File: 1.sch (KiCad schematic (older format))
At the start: 46 parts, among them J1 Micro_SD_Card, J10 BxI2C1, J11 I2C2, J2 USB_B_Micro, J3 Power, J4 SWD, J5 Protected, J6 SPI1, J7 ADC, J8 UART1, J9 SPI2, K1 NRST, K2 WKUP, K3 KPA0, U1 STM32F103C8Tx, U2 AMS1117-3.3, Y1 8MHz, Y2 32.768k

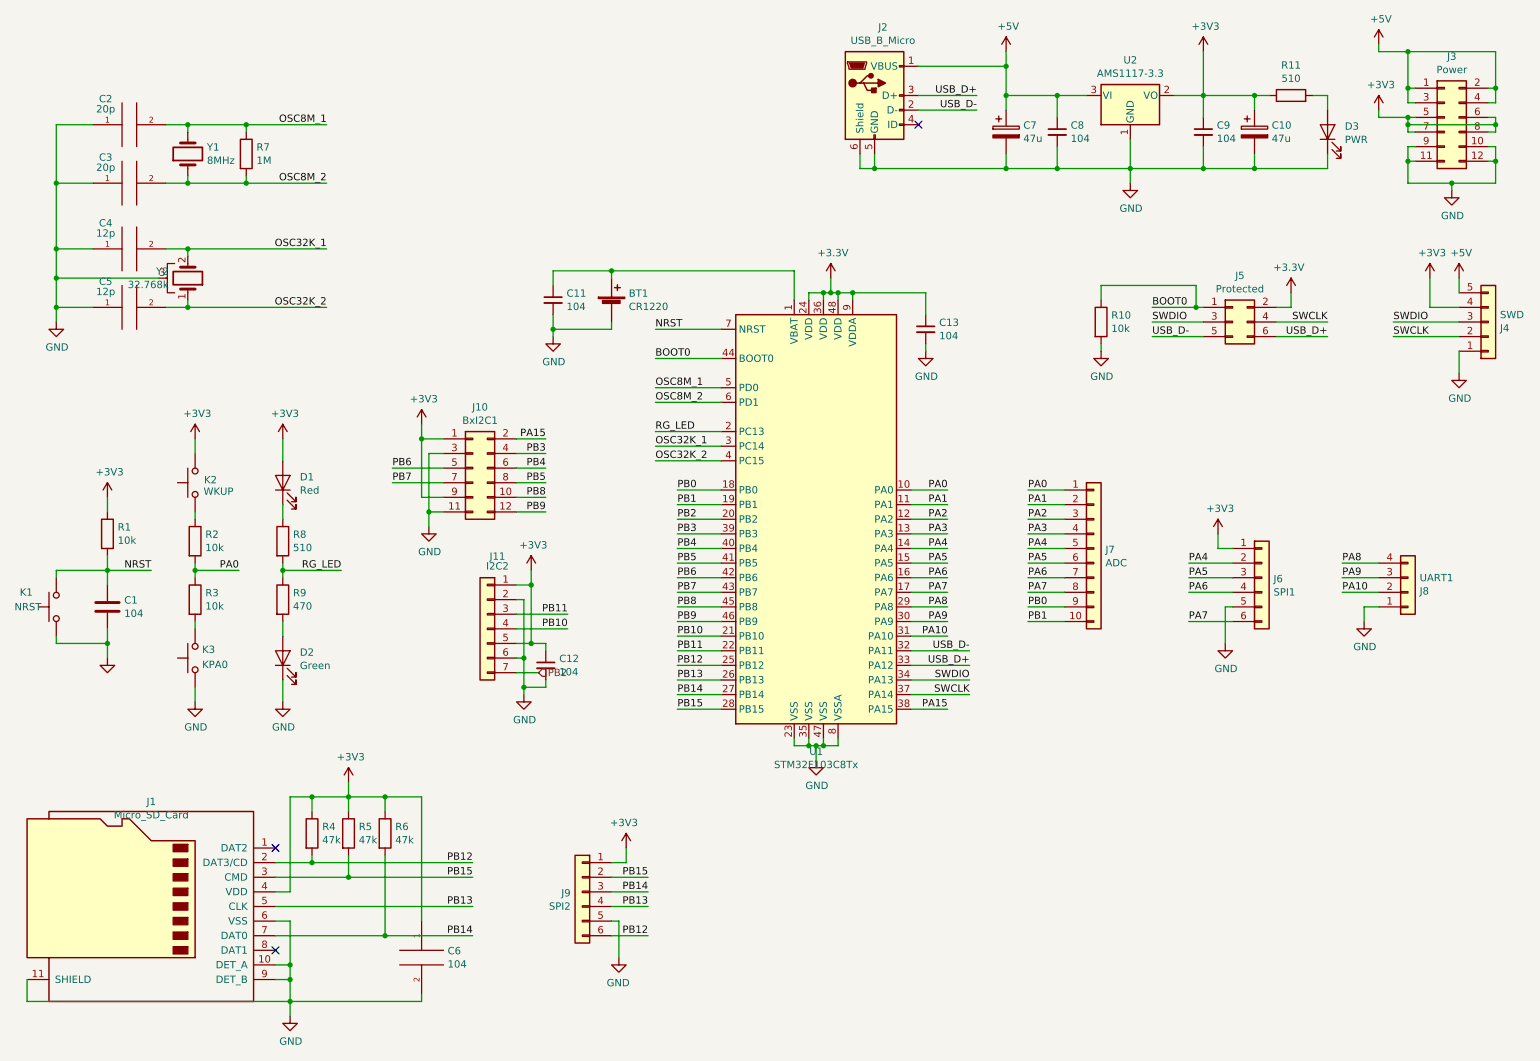
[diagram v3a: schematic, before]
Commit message: 修改原理图字段，并修改PCB
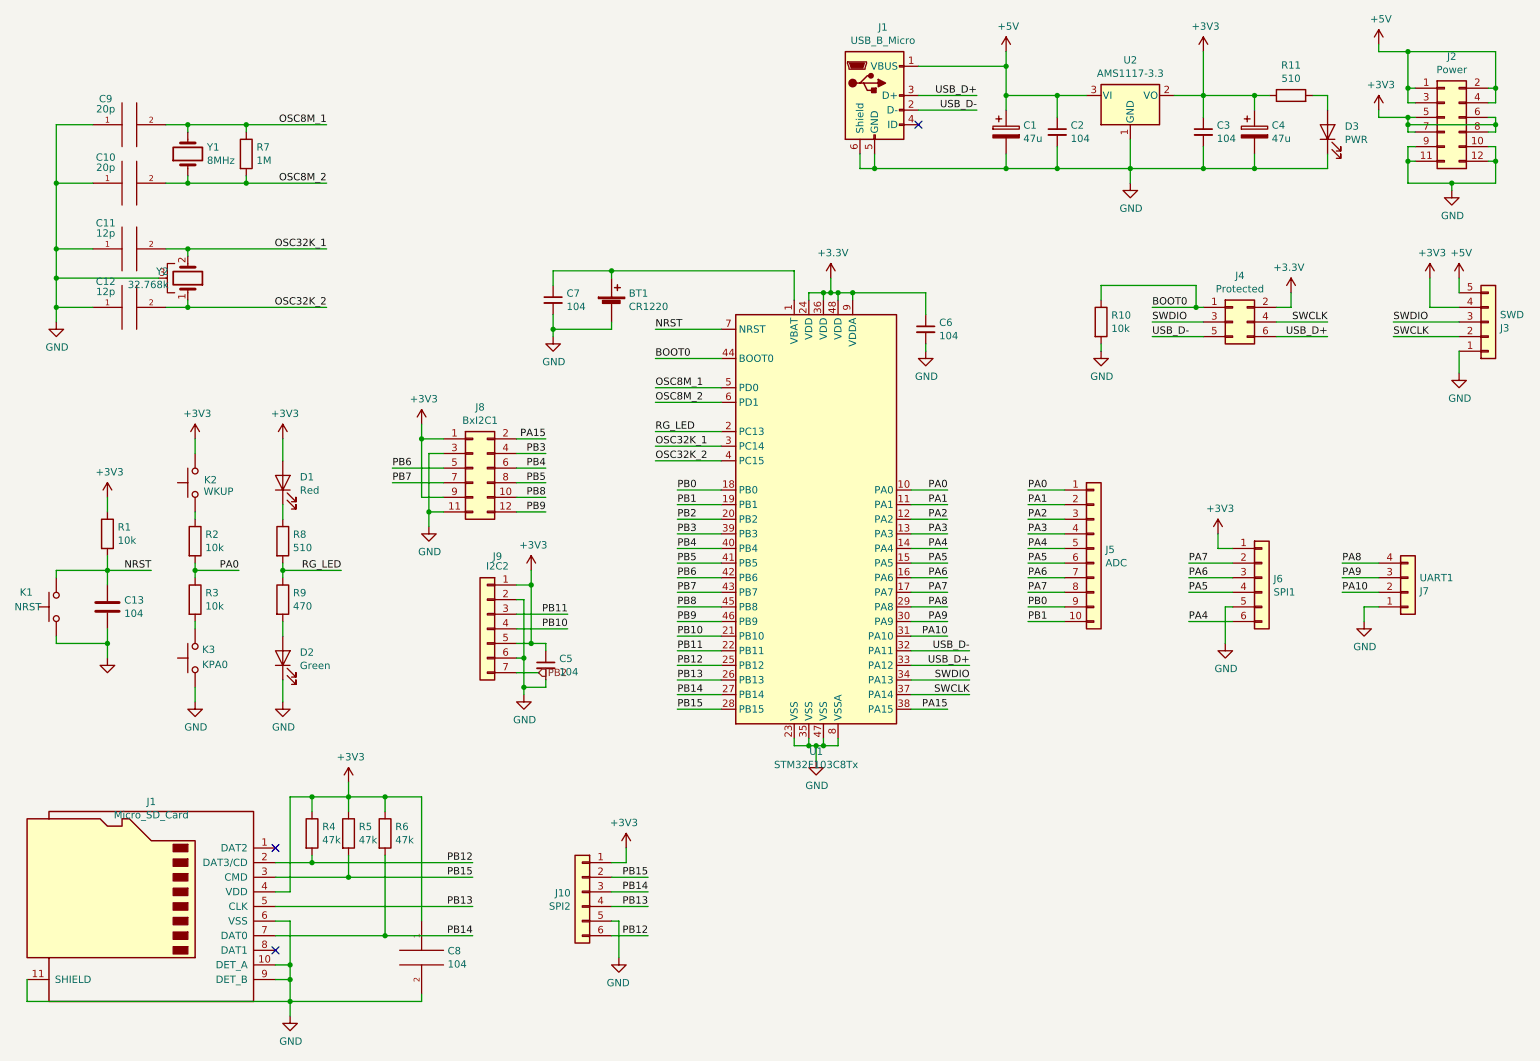
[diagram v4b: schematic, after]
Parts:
- C5: renamed from C12; footprint Capacitor_SMD:C_0201_0603Metric -> Capacitor_SMD:C_0603_1608Metric
- renumbered C7 to C1, C3 to C10, C4 to C11, C5 to C12, C1 to C13, C8 to C2, C9 to C3, C10 to C4, C13 to C6, C11 to C7, C6 to C8, C2 to C9, J2 to J1, J9 to J10, J3 to J2, J4 to J3, J5 to J4, J7 to J5, J8 to J7, J10 to J8, J11 to J9
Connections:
- net PA4: now also J6.6 (Pin_6); no longer J6.2 (Pin_2)
- net PA5: now also J6.4 (Pin_4); no longer J6.3 (Pin_3)
- net PA6: now also J6.3 (Pin_3); no longer J6.4 (Pin_4)
- net PA7: now also J6.2 (Pin_2); no longer J6.6 (Pin_6)
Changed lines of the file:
@@
 $EndComp
 $Comp
-L Device:C C1
+L Device:C C13
 U 1 1 60803DC4
 P 1350 4750
-F 0 "C1" H 1465 4796 50  0000 L CNN
+F 0 "C13" H 1465 4796 50  0000 L CNN
 F 1 "104" H 1465 4705 50  0000 L CNN
 F 2 "Capacitor_SMD:C_0603_1608Metric" H 1388 4600 50  0001 C CNN
@@
 	1250 1450 1000 1450
 $Comp
-L pspice:CAP C2
+L pspice:CAP C9
 U 1 1 60899DE9
 P 1500 1450
-F 0 "C2" V 1706 1612 50  0000 C BNN
+F 0 "C9" V 1706 1612 50  0000 C BNN
 F 1 "20p" V 1607 1612 50  0000 C CNN
 F 2 "Capacitor_SMD:C_0603_1608Metric" H 1500 1450 50  0001 C CNN
@@
 	1000 1450 1000 1850
 $Comp
-L pspice:CAP C3
+L pspice:CAP C10
 U 1 1 6092BDFE
 P 1500 1850
-F 0 "C3" V 1706 2012 50  0000 C BNN
+F 0 "C10" V 1706 2012 50  0000 C BNN
 F 1 "20p" V 1607 2012 50  0000 C CNN
 F 2 "Capacitor_SMD:C_0603_1608Metric" H 1500 1850 50  0001 C CNN
@@
 $EndComp
 $Comp
-L pspice:CAP C4
+L pspice:CAP C11
 U 1 1 6092C5E0
 P 1500 2300
-F 0 "C4" V 1706 2462 50  0000 C BNN
+F 0 "C11" V 1706 2462 50  0000 C BNN
 F 1 "12p" V 1607 2462 50  0000 C CNN
 F 2 "Capacitor_SMD:C_0603_1608Metric" H 1500 2300 50  0001 C CNN
@@
 $EndComp
 $Comp
-L pspice:CAP C5
+L pspice:CAP C12
 U 1 1 6092D115
 P 1500 2700
-F 0 "C5" V 1706 2862 50  0000 C BNN
+F 0 "C12" V 1706 2862 50  0000 C BNN
 F 1 "12p" V 1607 2862 50  0000 C CNN
 F 2 "Capacitor_SMD:C_0603_1608Metric" H 1500 2700 50  0001 C CNN
@@
 Connection ~ 3250 6050
 $Comp
-L pspice:C C6
+L pspice:C C8
 U 1 1 60A0DA04
 P 3500 7150
-F 0 "C6" H 3678 7196 50  0000 L CNN
+F 0 "C8" H 3678 7196 50  0000 L CNN
 F 1 "104" H 3678 7105 50  0000 L CNN
 F 2 "Capacitor_SMD:C_0603_1608Metric" H 3500 7150 50  0001 C CNN
@@
 $EndComp
 $Comp
-L Connector_Generic:Conn_02x03_Odd_Even J5
+L Connector_Generic:Conn_02x03_Odd_Even J4
 U 1 1 608D3B31
 P 9050 2800
-F 0 "J5" H 9100 3117 50  0000 C CNN
+F 0 "J4" H 9100 3117 50  0000 C CNN
 F 1 "Protected" H 9100 3026 50  0000 C CNN
 F 2 "Connector_PinHeader_2.54mm:PinHeader_2x03_P2.54mm_Vertical" H 9050 2800 50  0001 C CNN
@@
 	9000 4750 9000 5000
 $Comp
-L Connector_Generic:Conn_01x10 J7
+L Connector_Generic:Conn_01x10 J5
 U 1 1 60BF7B89
 P 8100 4350
-F 0 "J7" H 8180 4342 50  0000 L CNN
+F 0 "J5" H 8180 4342 50  0000 L CNN
 F 1 "ADC" H 8180 4251 50  0000 L CNN
 F 2 "Connector_PinHeader_2.54mm:PinHeader_1x10_P2.54mm_Vertical" H 8100 4350 50  0001 C CNN
@@
 $EndComp
 $Comp
-L Connector_Generic:Conn_01x04 J8
+L Connector_Generic:Conn_01x04 J7
 U 1 1 60F3F899
 P 10250 4650
-F 0 "J8" H 10330 4642 50  0000 L CNN
+F 0 "J7" H 10330 4642 50  0000 L CNN
 F 1 "UART1" H 10330 4551 50  0000 L CNN
 F 2 "Connector_PinHeader_2.54mm:PinHeader_1x04_P2.54mm_Vertical" H 10250 4650 50  0001 C CNN
@@
 $EndComp
 $Comp
-L Device:C_Small C11
+L Device:C_Small C7
 U 1 1 6096DC0F
 P 4400 2650
-F 0 "C11" H 4492 2696 50  0000 L CNN
+F 0 "C7" H 4492 2696 50  0000 L CNN
 F 1 "104" H 4492 2605 50  0000 L CNN
 F 2 "Capacitor_SMD:C_0603_1608Metric" H 4400 2650 50  0001 C CNN
@@
 	4400 2850 4400 2900
 $Comp
-L Device:C_Small C13
+L Device:C_Small C6
 U 1 1 60A78AA2
 P 6950 2850
-F 0 "C13" H 7042 2896 50  0000 L CNN
+F 0 "C6" H 7042 2896 50  0000 L CNN
 F 1 "104" H 7042 2805 50  0000 L CNN
 F 2 "Capacitor_SMD:C_0603_1608Metric" H 6950 2850 50  0001 C CNN
@@
 	10600 2500 10600 2600
 $Comp
-L Connector_Generic:Conn_01x05 J4
+L Connector_Generic:Conn_01x05 J3
 U 1 1 60DF5E87
 P 10800 2800
-F 0 "J4" H 10880 2842 50  0000 L CNN
+F 0 "J3" H 10880 2842 50  0000 L CNN
 F 1 "SWD" H 10880 2751 50  0000 L CNN
 F 2 "Connector_PinHeader_2.54mm:PinHeader_1x05_P2.54mm_Horizontal" H 10800 2800 50  0001 C CNN
@@
 $EndComp
 $Comp
-L Connector_Generic:Conn_02x06_Odd_Even J3
+L Connector_Generic:Conn_02x06_Odd_Even J2
 U 1 1 60CA00CD
 P 10500 1400
-F 0 "J3" H 10550 1817 50  0000 C CNN
+F 0 "J2" H 10550 1817 50  0000 C CNN
 F 1 "Power" H 10550 1726 50  0000 C CNN
 F 2 "Connector_PinHeader_2.54mm:PinHeader_2x06_P2.54mm_Vertical" H 10500 1400 50  0001 C CNN
@@
 $EndComp
 $Comp
-L Connector:USB_B_Micro J2
+L Connector:USB_B_Micro J1
 U 1 1 60B0F0BF
 P 6600 1250
-F 0 "J2" H 6657 1717 50  0000 C CNN
+F 0 "J1" H 6657 1717 50  0000 C CNN
 F 1 "USB_B_Micro" H 6657 1626 50  0000 C CNN
 F 2 "Connector_USB:USB_Micro-B_GCT_USB3076-30-A" H 6750 1200 50  0001 C CNN
@@
 	8650 1250 8850 1250
 $Comp
-L Device:CP C10
+L Device:CP C4
 U 1 1 60B9D540
 P 9200 1500
-F 0 "C10" H 9318 1546 50  0000 L CNN
+F 0 "C4" H 9318 1546 50  0000 L CNN
 F 1 "47u" H 9318 1455 50  0000 L CNN
 F 2 "Capacitor_SMD:C_1206_3216Metric" H 9238 1350 50  0001 C CNN
@@
 	7850 1250 7850 1400
 $Comp
-L Device:C_Small C9
+L Device:C_Small C3
 U 1 1 60B7BA0C
 P 8850 1500
-F 0 "C9" H 8942 1546 50  0000 L CNN
+F 0 "C3" H 8942 1546 50  0000 L CNN
 F 1 "104" H 8942 1455 50  0000 L CNN
 F 2 "Capacitor_SMD:C_0603_1608Metric" H 8850 1500 50  0001 C CNN
@@
 $EndComp
 $Comp
-L Device:C_Small C8
+L Device:C_Small C2
 U 1 1 60B7A582
 P 7850 1500
-F 0 "C8" H 7942 1546 50  0000 L CNN
+F 0 "C2" H 7942 1546 50  0000 L CNN
 F 1 "104" H 7942 1455 50  0000 L CNN
 F 2 "Capacitor_SMD:C_0603_1608Metric" H 7850 1500 50  0001 C CNN
@@
 $EndComp
 $Comp
-L Device:CP C7
+L Device:CP C1
 U 1 1 60B79A0D
 P 7500 1500
-F 0 "C7" H 7618 1546 50  0000 L CNN
+F 0 "C1" H 7618 1546 50  0000 L CNN
 F 1 "47u" H 7618 1455 50  0000 L CNN
 F 2 "Capacitor_SMD:C_1206_3216Metric" H 7538 1350 50  0001 C CNN
@@
 	3500 3600 3650 3600
 $Comp
-L Connector_Generic:Conn_02x06_Odd_Even J10
+L Connector_Generic:Conn_02x06_Odd_Even J8
 U 1 1 60B34FEB
 P 3850 3800
-F 0 "J10" H 3900 4217 50  0000 C CNN
+F 0 "J8" H 3900 4217 50  0000 C CNN
 F 1 "BxI2C1" H 3900 4126 50  0000 C CNN
 F 2 "Connector_PinHeader_2.54mm:PinHeader_2x06_P2.54mm_Vertical" H 3850 3800 50  0001 C CNN
@@
 	4800 6900 4850 6900
 $Comp
-L Connector_Generic:Conn_01x06 J9
+L Connector_Generic:Conn_01x06 J10
 U 1 1 61009C91
 P 4600 6700
-F 0 "J9" H 4680 6692 50  0000 L CNN
+F 0 "J10" H 4680 6692 50  0000 L CNN
 F 1 "SPI2" H 4680 6601 50  0000 L CNN
 F 2 "Connector_PinHeader_2.54mm:PinHeader_1x06_P2.54mm_Vertical" H 4680 6555 50  0001 L CNN
@@
 	4350 5050 4350 5000
 $Comp
-L Device:C_Small C12
+L Device:C_Small C5
 U 1 1 609EBE25
 P 4350 5150
-F 0 "C12" H 4442 5196 50  0000 L CNN
+F 0 "C5" H 4442 5196 50  0000 L CNN
 F 1 "104" H 4442 5105 50  0000 L CNN
-F 2 "Capacitor_SMD:C_0201_0603Metric" H 4350 5150 50  0001 C CNN
+F 2 "Capacitor_SMD:C_0603_1608Metric" H 4350 5150 50  0001 C CNN
 F 3 "~" H 4350 5150 50  0001 C CNN
 	1    4350 5150
@@
 	4150 5100 4200 5100
 $Comp
-L Connector_Generic:Conn_01x07 J11
+L Connector_Generic:Conn_01x07 J9
 U 1 1 6153FBE5
 P 3950 4900
-F 0 "J11" H 3881 5396 50  0000 C CNN
+F 0 "J9" H 3881 5396 50  0000 C CNN
 F 1 "I2C2" H 3881 5329 50  0000 C CNN
 F 2 "Connector_PinHeader_2.54mm:PinHeader_1x07_P2.54mm_Vertical" H 3950 4900 50  0001 C CNN
@@
 	7650 4850 7900 4850
 Text Label 8750 4450 0    50   ~ 0
+PA7
+Text Label 8750 4550 0    50   ~ 0
+PA6
+Text Label 8750 4650 0    50   ~ 0
+PA5
+Text Label 8750 4850 0    50   ~ 0
 PA4
-Text Label 8750 4550 0    50   ~ 0
-PA5
-Text Label 8750 4650 0    50   ~ 0
-PA6
-Text Label 8750 4850 0    50   ~ 0
-PA7
 Wire Wire Line
 	8750 4650 9050 4650

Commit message: 修改字段2
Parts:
- renumbered J1 to J11
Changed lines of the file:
@@
-$EndComp
-$Comp
-L power:GND #PWR0105
-U 1 1 608A3AFC
-P 1000 2800
-F 0 "#PWR0105" H 1000 2550 50  0001 C CNN
-F 1 "GND" H 1005 2627 50  0000 C CNN
-F 2 "" H 1000 2800 50  0001 C CNN
-F 3 "" H 1000 2800 50  0001 C CNN
-	1    1000 2800
-	1    0    0    -1
 $EndComp
 $Comp
@@
 	1750 1450 1900 1450
 Wire Wire Line
-	1250 1450 1000 1450
-$Comp
-L pspice:CAP C9
-U 1 1 60899DE9
-P 1500 1450
-F 0 "C9" V 1706 1612 50  0000 C BNN
-F 1 "20p" V 1607 1612 50  0000 C CNN
-F 2 "Capacitor_SMD:C_0603_1608Metric" H 1500 1450 50  0001 C CNN
-F 3 "~" H 1500 1450 50  0001 C CNN
-	1    1500 1450
-	0    -1   -1   0
-$EndComp
-Wire Wire Line
-	1000 1450 1000 1850
-$Comp
-L pspice:CAP C10
-U 1 1 6092BDFE
-P 1500 1850
-F 0 "C10" V 1706 2012 50  0000 C BNN
-F 1 "20p" V 1607 2012 50  0000 C CNN
-F 2 "Capacitor_SMD:C_0603_1608Metric" H 1500 1850 50  0001 C CNN
-F 3 "~" H 1500 1850 50  0001 C CNN
-	1    1500 1850
-	0    -1   -1   0
-$EndComp
-$Comp
-L pspice:CAP C11
-U 1 1 6092C5E0
-P 1500 2300
-F 0 "C11" V 1706 2462 50  0000 C BNN
-F 1 "12p" V 1607 2462 50  0000 C CNN
-F 2 "Capacitor_SMD:C_0603_1608Metric" H 1500 2300 50  0001 C CNN
-F 3 "~" H 1500 2300 50  0001 C CNN
-	1    1500 2300
-	0    -1   -1   0
-$EndComp
-$Comp
-L pspice:CAP C12
-U 1 1 6092D115
-P 1500 2700
-F 0 "C12" V 1706 2862 50  0000 C BNN
-F 1 "12p" V 1607 2862 50  0000 C CNN
-F 2 "Capacitor_SMD:C_0603_1608Metric" H 1500 2700 50  0001 C CNN
-F 3 "~" H 1500 2700 50  0001 C CNN
-	1    1500 2700
-	0    -1   -1   0
-$EndComp
-Wire Wire Line
-	1250 1850 1000 1850
-Connection ~ 1000 1850
-Wire Wire Line
-	1000 1850 1000 2300
-Wire Wire Line
-	1250 2300 1000 2300
-Connection ~ 1000 2300
-Wire Wire Line
-	1000 2300 1000 2500
-Wire Wire Line
-	1250 2700 1000 2700
-Connection ~ 1000 2700
-Wire Wire Line
-	1000 2700 1000 2800
-Wire Wire Line
 	2500 6600 3000 6600
 Wire Wire Line
@@
 	3500 6050 3500 6900
 Connection ~ 3250 6050
-$Comp
-L pspice:C C8
-U 1 1 60A0DA04
-P 3500 7150
-F 0 "C8" H 3678 7196 50  0000 L CNN
-F 1 "104" H 3678 7105 50  0000 L CNN
-F 2 "Capacitor_SMD:C_0603_1608Metric" H 3500 7150 50  0001 C CNN
-F 3 "~" H 3500 7150 50  0001 C CNN
-	1    3500 7150
-	1    0    0    -1
-$EndComp
 Wire Wire Line
 	2600 7450 3500 7450
@@
 	1750 2700 1900 2700
 $Comp
-L Connector:Micro_SD_Card_Det J1
+L Connector:Micro_SD_Card_Det J11
 U 1 1 60953440
 P 1600 6800
-F 0 "J1" H 1550 7517 50  0000 C CNN
+F 0 "J11" H 1550 7517 50  0000 C CNN
 F 1 "Micro_SD_Card" H 1550 7426 50  0000 C CNN
 F 2 "Connector_Card:microSD_HC_Hirose_DM3BT-DSF-PEJS" H 2750 7100 50  0001 C CNN
@@
 	-1   0    0    -1
 $EndComp
-Wire Wire Line
-	1700 2500 1000 2500
-Connection ~ 1000 2500
-Wire Wire Line
-	1000 2500 1000 2700
 Wire Wire Line
 	800  7300 800  7450
@@
 Wire Wire Line
 	9350 2900 9700 2900
+Wire Wire Line
+	1000 2500 1000 2700
+Connection ~ 1000 2500
+Wire Wire Line
+	1700 2500 1000 2500
+Wire Wire Line
+	1000 2700 1000 2800
+Connection ~ 1000 2700
+Wire Wire Line
+	1250 2700 1000 2700
+Wire Wire Line
+	1000 2300 1000 2500
+Connection ~ 1000 2300
+Wire Wire Line
+	1250 2300 1000 2300
+Wire Wire Line
+	1000 1850 1000 2300
+Connection ~ 1000 1850
+Wire Wire Line
+	1250 1850 1000 1850
+Wire Wire Line
+	1000 1450 1000 1850
+Wire Wire Line
+	1250 1450 1000 1450
+$Comp
+L power:GND #PWR0105
+U 1 1 608A3AFC
+P 1000 2800
+F 0 "#PWR0105" H 1000 2550 50  0001 C CNN
+F 1 "GND" H 1005 2627 50  0000 C CNN
+F 2 "" H 1000 2800 50  0001 C CNN
+F 3 "" H 1000 2800 50  0001 C CNN
+	1    1000 2800
+	1    0    0    -1
+$EndComp
+$Comp
+L pspice:CAP C12
+U 1 1 6092D115
+P 1500 2700
+F 0 "C12" V 1706 2862 50  0000 C BNN
+F 1 "12p" V 1607 2862 50  0000 C CNN
+F 2 "Capacitor_SMD:C_0603_1608Metric" H 1500 2700 50  0001 C CNN
+F 3 "~" H 1500 2700 50  0001 C CNN
+	1    1500 2700
+	0    -1   -1   0
+$EndComp
+$Comp
+L pspice:CAP C11
+U 1 1 6092C5E0
+P 1500 2300
+F 0 "C11" V 1706 2462 50  0000 C BNN
+F 1 "12p" V 1607 2462 50  0000 C CNN
+F 2 "Capacitor_SMD:C_0603_1608Metric" H 1500 2300 50  0001 C CNN
+F 3 "~" H 1500 2300 50  0001 C CNN
+	1    1500 2300
+	0    -1   -1   0
+$EndComp
+$Comp
+L pspice:CAP C10
+U 1 1 6092BDFE
+P 1500 1850
+F 0 "C10" V 1706 2012 50  0000 C BNN
+F 1 "20p" V 1607 2012 50  0000 C CNN
+F 2 "Capacitor_SMD:C_0603_1608Metric" H 1500 1850 50  0001 C CNN
+F 3 "~" H 1500 1850 50  0001 C CNN
+	1    1500 1850
+	0    -1   -1   0
+$EndComp
+$Comp
+L pspice:CAP C9
+U 1 1 60899DE9
+P 1500 1450
+F 0 "C9" V 1706 1612 50  0000 C BNN
+F 1 "20p" V 1607 1612 50  0000 C CNN
+F 2 "Capacitor_SMD:C_0603_1608Metric" H 1500 1450 50  0001 C CNN
+F 3 "~" H 1500 1450 50  0001 C CNN
+	1    1500 1450
+	0    -1   -1   0
+$EndComp
+$Comp
+L pspice:C C8
+U 1 1 60A0DA04
+P 3500 7150
+F 0 "C8" H 3678 7196 50  0000 L CNN
+F 1 "104" H 3678 7105 50  0000 L CNN
+F 2 "Capacitor_SMD:C_0603_1608Metric" H 3500 7150 50  0001 C CNN
+F 3 "~" H 3500 7150 50  0001 C CNN
+	1    3500 7150
+	1    0    0    -1
+$EndComp
 $EndSCHEMATC

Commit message: move 32.768k OSC
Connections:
- net OSC32K_1: now also Y2.1; no longer Y2.2
- net OSC32K_2: now also Y2.2; no longer Y2.1
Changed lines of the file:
@@
 F 3 "~" H 1900 2500 50  0001 C CNN
 	1    1900 2500
-	0    1    -1   0
+	0    1    1    0
 $EndComp
 $Comp
